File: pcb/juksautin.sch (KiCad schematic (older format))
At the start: 18 parts, among them J1 Screw_Terminal_01x09, J2 ATMEGA32U4 pin 42, U1 SP3485CN, U2 LM4041

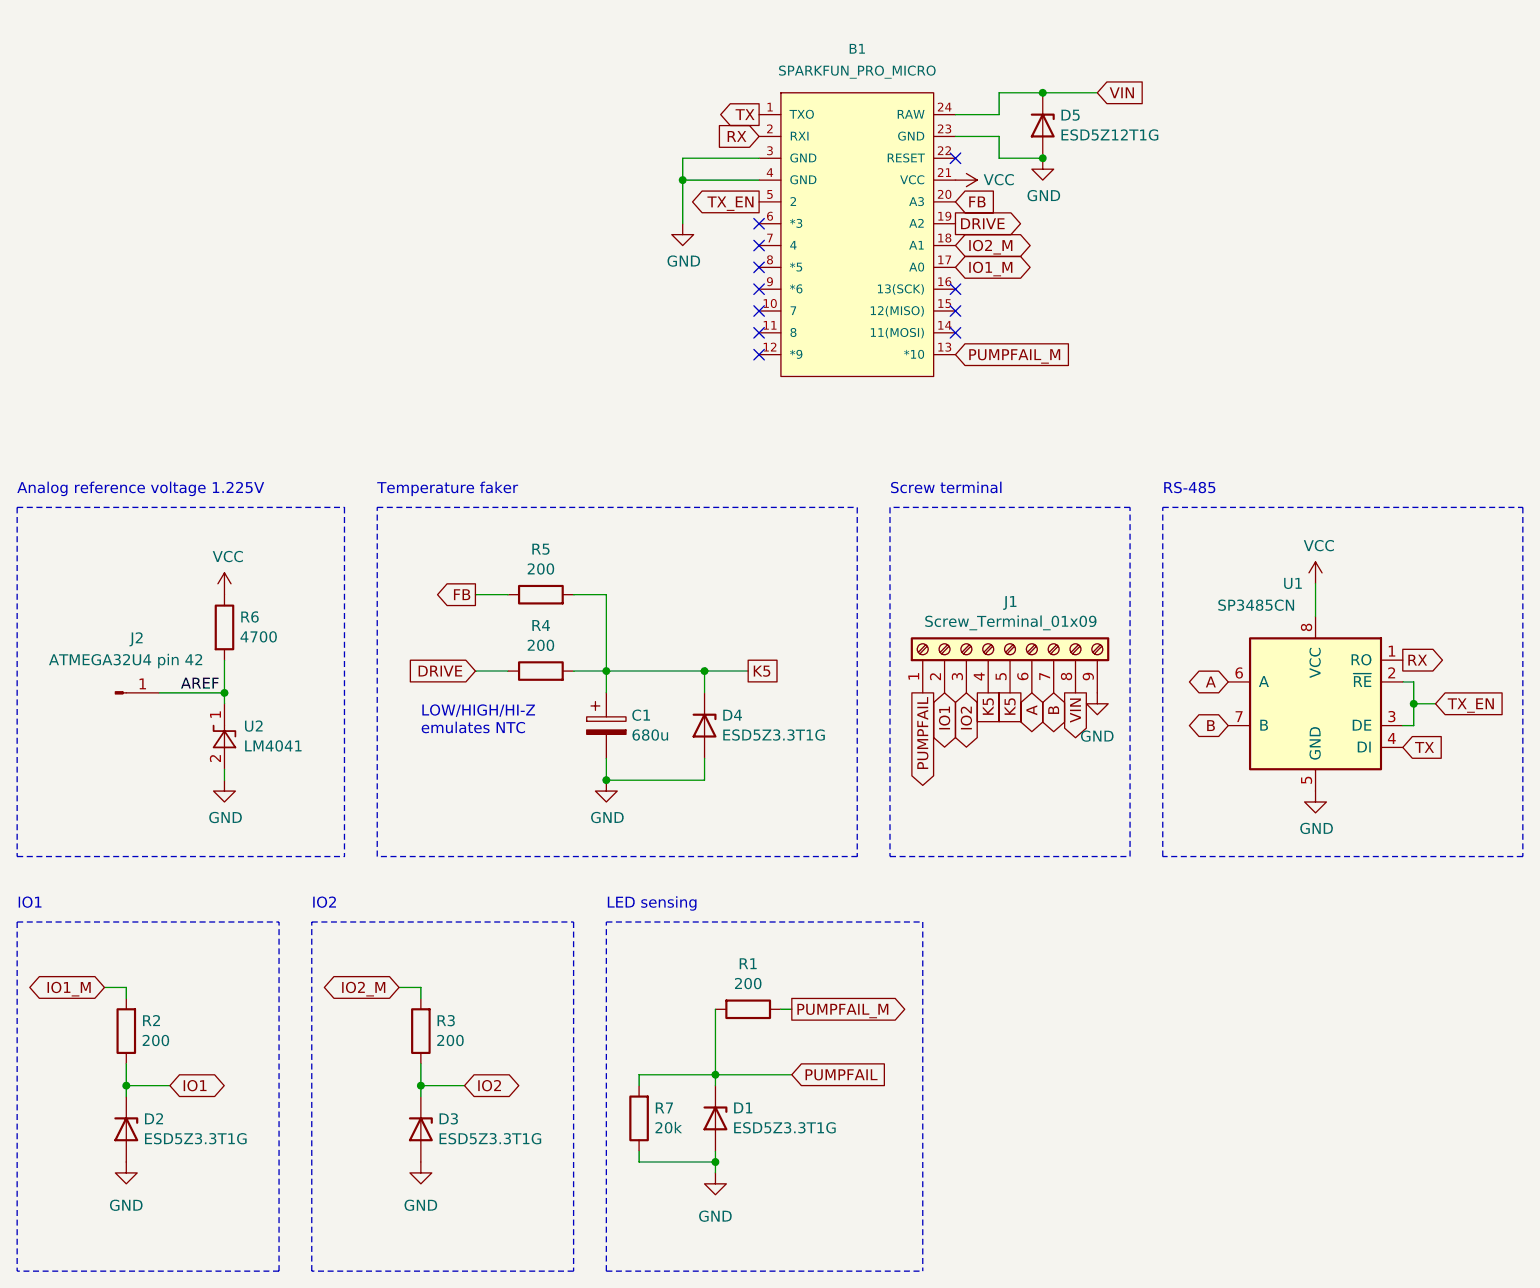
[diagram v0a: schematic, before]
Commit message: Support 24VDC input
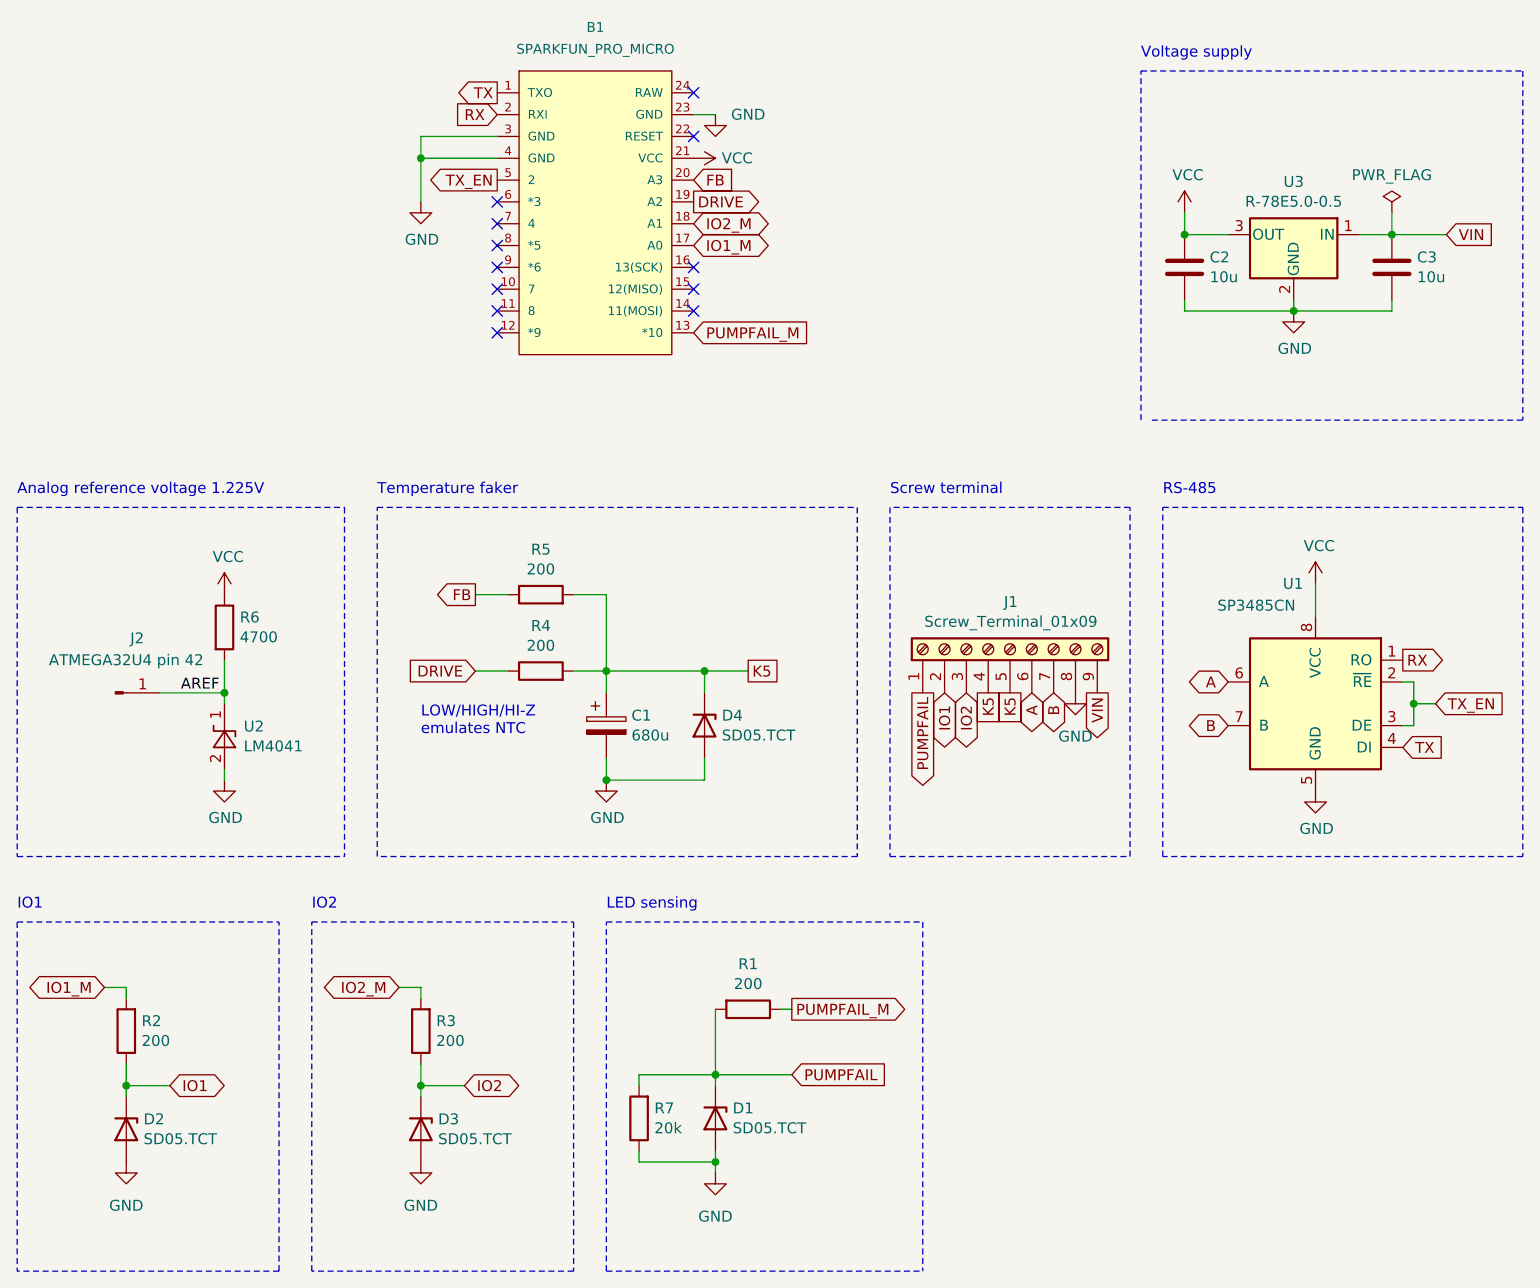
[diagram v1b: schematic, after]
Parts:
- removed D5: ESD5Z12T1G, Diode_SMD:D_SOD-523, symbol Diode:DZ2S039X0L
- added C2, C3: 10u, Capacitor_SMD:C_1206_3216Metric_Pad1.33x1.80mm_HandSolder, symbol Device:C
- added U3: R-78E5.0-0.5, Converter_DCDC:Converter_DCDC_RECOM_R-78E-0.5_THT, symbol Regulator_Switching:R-78E5.0-0.5
- D1, D2, D3, D4: value ESD5Z3.3T1G -> SD05.TCT; footprint Diode_SMD:D_SOD-523 -> Diode_SMD:D_SOD-323_HandSoldering
- J2: footprint Connector_PinHeader_2.54mm:PinHeader_1x01_P2.54mm_Vertical -> Connector_Wire:SolderWire-0.5sqmm_1x01_D0.9mm_OD2.1mm
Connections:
- net GND: now also J1.8 (Pin_8), C2.2, C3.2, U3.2 (GND); no longer J1.9 (Pin_9)
- net VCC: now also C2.1, U3.3 (OUT)
- net VIN: now also J1.9 (Pin_9), C3.1, U3.1 (IN); no longer B1.24 (RAW), J1.8 (Pin_8)
- no-connect marks 11 -> 12
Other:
- note added: "Voltage supply"
- moved on the sheet: B1

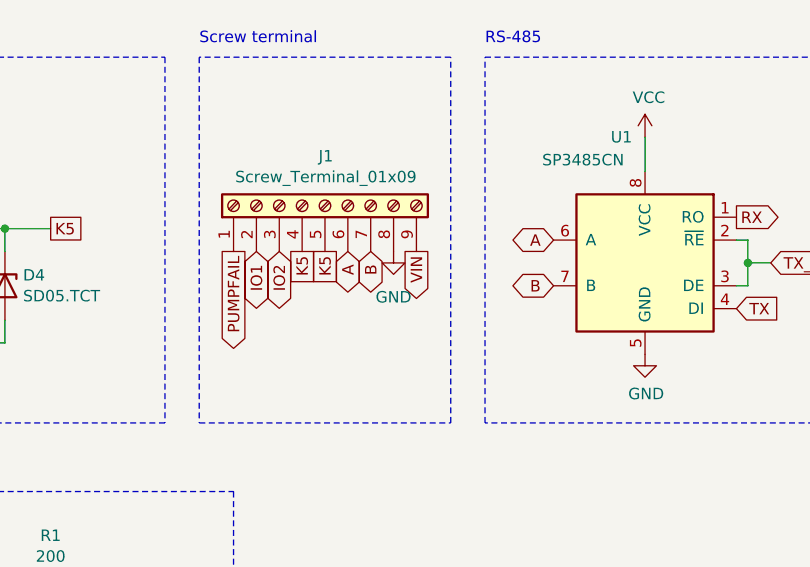
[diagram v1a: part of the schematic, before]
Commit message: pcb: Make the board two-layer instead of one
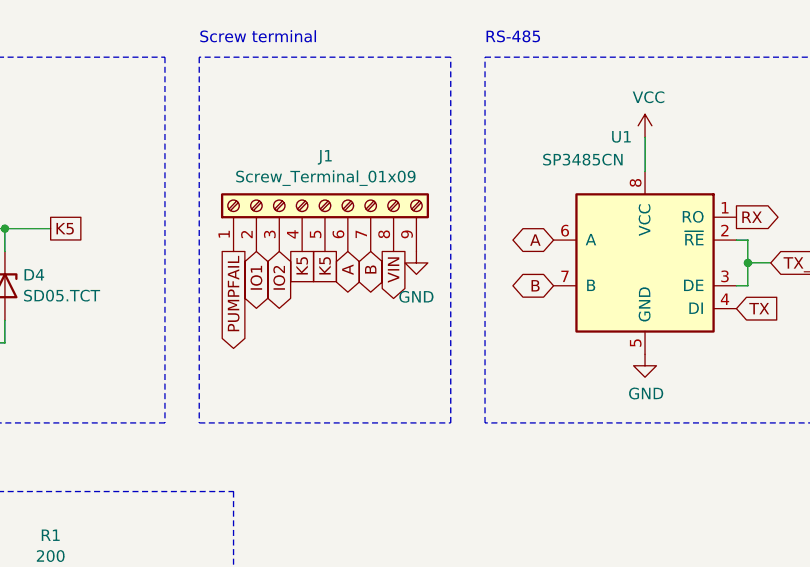
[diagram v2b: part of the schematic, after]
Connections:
- net GND: now also J1.9 (Pin_9); no longer J1.8 (Pin_8)
- net VIN: now also J1.8 (Pin_8); no longer J1.9 (Pin_9)
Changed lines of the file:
@@
 Sheet 1 1
 Title "Pumpunjuksautin"
-Date "2021-05-24"
-Rev "0.6"
+Date "2021-05-28"
+Rev "0.7"
 Comp "Oy Pula-ajan Puhelin Ab"
 Comment1 ""
@@
 L power:GND #PWR0108
 U 1 1 61456AC1
-P 6550 4550
-F 0 "#PWR0108" H 6550 4300 50  0001 C CNN
-F 1 "GND" H 6550 4350 50  0000 C CNN
-F 2 "" H 6550 4550 50  0001 C CNN
-F 3 "" H 6550 4550 50  0001 C CNN
-	1    6550 4550
-	1    0    0    -1
-$EndComp
-Text GLabel 6650 4550 3    50   Output ~ 0
+P 6650 4550
+F 0 "#PWR0108" H 6650 4300 50  0001 C CNN
+F 1 "GND" H 6650 4350 50  0000 C CNN
+F 2 "" H 6650 4550 50  0001 C CNN
+F 3 "" H 6650 4550 50  0001 C CNN
+	1    6650 4550
+	1    0    0    -1
+$EndComp
+Text GLabel 6550 4550 3    50   Output ~ 0
 VIN
 Text GLabel 8250 2450 2    50   Input ~ 0
